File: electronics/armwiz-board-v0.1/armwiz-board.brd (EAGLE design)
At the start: 99.1 x 51.5 mm, 135 parts, among them IC1 STM32F_48PIN, IC2 TXS0108, IC3 TLV70033DCK, J1 MICRO-SDCARD-CONNECTOR-330006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, J15 Cortex Debug, J16 ST-Link v2, J2 CORTEX_DEBUGSMD, Q1 IRLML5103, U1 STM32F10XRXT6, U4 MIC5219-3.3V, X1 FH12-12S-1S, Y1 8MHz, Y3 32.768kHz

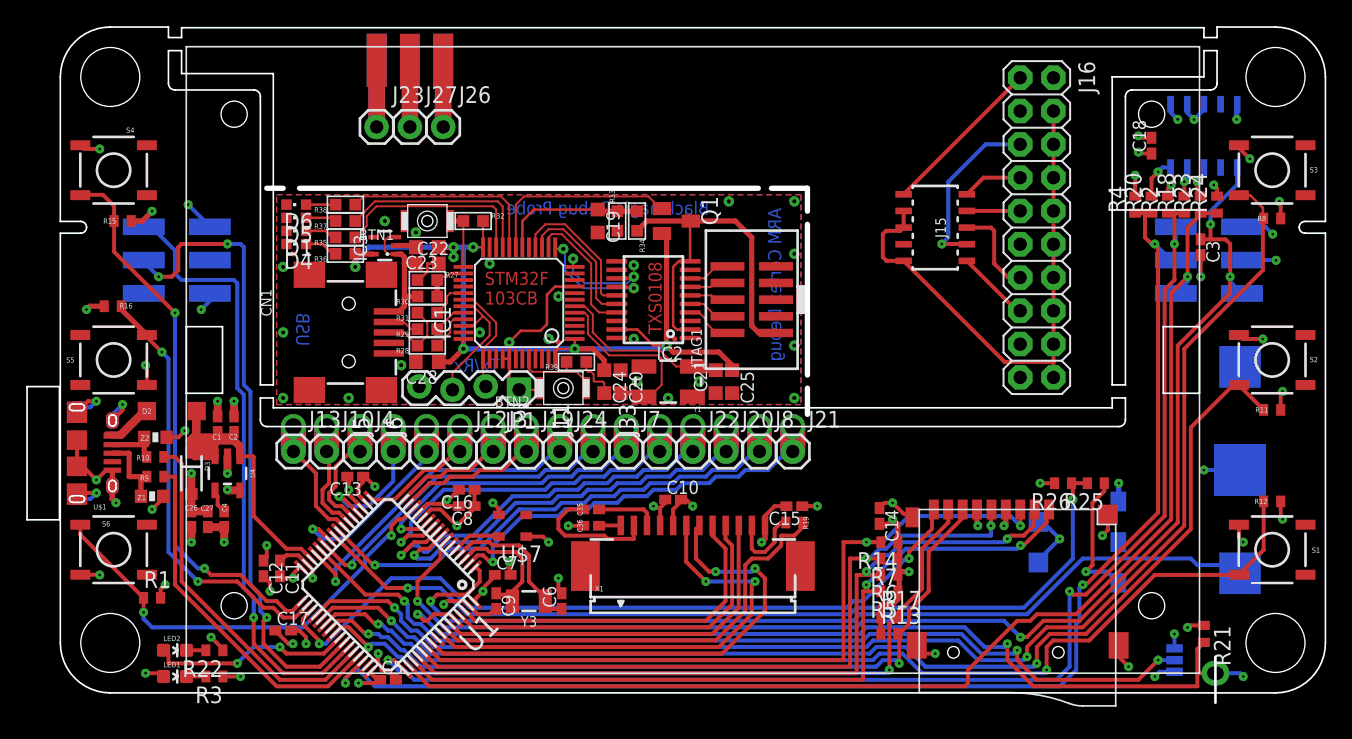
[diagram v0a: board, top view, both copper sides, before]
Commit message: Fixed an issue. Traces were going through the LCD cutout.
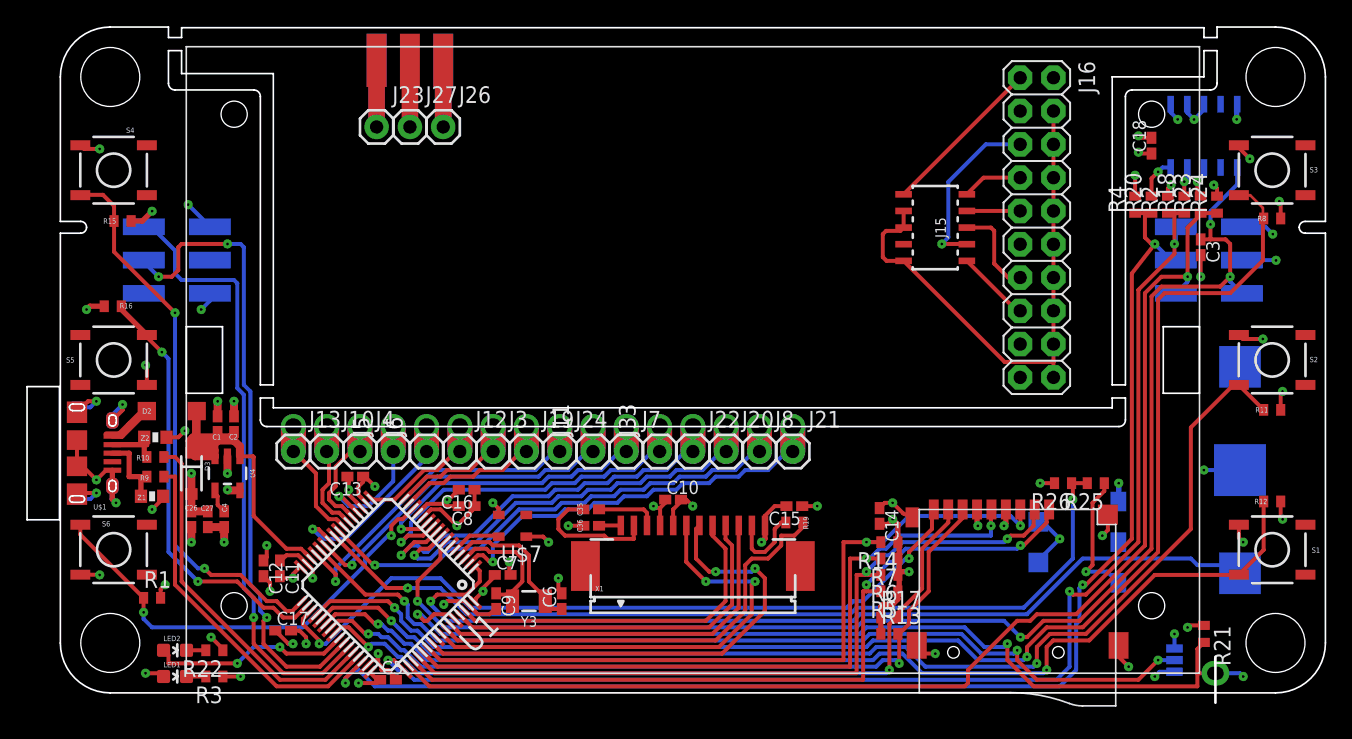
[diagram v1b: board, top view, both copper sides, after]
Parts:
- removed BTN1, BTN2: SPST.B3U-1000P(M)-B, omron:B3U-1000P(M)-B
- removed C19, C24, C25, C28: 100nF, resistor:C0603K
- removed C20, C21: 18pF, resistor:C0603K
- removed C22, C23: 1µF, resistor:C0603K
- removed CN1: (no value), microbuilder_v3:USB-MINIB
- removed D1: RED, led:CHIPLED_0603
- removed D4: GREEN, led:CHIPLED_0603
- removed D5, D6: YELLOW, led:CHIPLED_0603
- removed IC1: STM32F_48PIN, stm32f:TQFP48
- removed IC2: TXS0108, dan-translate:TSSOP20
- removed IC3: TLV70033DCK, tlv700:SC70-5L
- removed JP1: (no value), SparkFun:1X04_LOCK
- removed JTAG1: (no value), microbuilder_v3:2X05_1.27MM_SMT
- removed Q1: IRLML5103, transistor-small-signal:SOT23
- removed R27, R32, R33, R39: 10K, microbuilder:0603-MINI
- removed R28, R29: 22Ω, microbuilder:0603-MINI
- removed R30, R34: 4K7, microbuilder:0603-MINI
- removed R31: 1K5, microbuilder:0603-MINI
- removed R35, R36, R37, R38: 390Ω, microbuilder:0603-MINI
- removed Y1: 8MHz, SparkFun:CRYSTAL-SMD-5X3
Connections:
- removed net 3.3V1: BTN2.2, C23.1, C24.1, C25.1, C28.1, IC1.1, IC1.24, IC1.36, IC1.40, IC1.41, IC1.48, IC1.9, IC2.19, IC3.5, JP1.1, Q1.2, R32.2, R36.1
- removed net 5.0V: C22.1, CN1.VBUS, IC3.1, IC3.3, R30.2
- removed net BOOT2: BTN2.1, IC1.44, R39.2
- removed net D+1: CN1.D+, R28.2, R31.2
- removed net D-1: CN1.D-, R29.2
- removed net FORCE_BOOTLOADER: BTN1.1, IC1.25, R32.1
- removed net GND1: BTN1.2, C19.2, C20.1, C21.1, C22.2, C23.2, C24.2, C25.2, C28.2, CN1.GND, CN1.ID, D1.C, D4.C, D5.C, D6.C, IC1.23, IC1.35, IC1.47, IC1.8, IC2.11, IC2.12, IC2.18, IC2.20, IC3.2, JP1.4, JTAG1.3, JTAG1.5, JTAG1.9, R27.1, R33.1, R39.1
- removed net LED0: IC1.20, R38.1
- removed net LED1: IC1.21, R37.1
- removed net LED2: IC1.22, R35.1
- removed net LPC_XTAL2: C21.2, IC1.6, Y1.1
- removed net N$10: D1.A, R35.2
- removed net N$17: D4.A, R36.2
- removed net N$25: D5.A, R37.2
- removed net N$26: D6.A, R38.2
- removed net OSC_IN1: C20.2, IC1.5, Y1.3
- removed net PWR_BR: IC1.19, Q1.1
- removed net RST: IC1.12, IC2.13
- removed net RXD: IC1.31, IC1.34, JP1.3
- removed net TARGET_POWER_ADC: C19.1, IC1.18, R33.2, R34.1
- removed net TARGET_RST: IC2.8, JTAG1.10
- removed net TARGET_TCK: IC2.5, JTAG1.4
- removed net TARGET_TDI: IC2.7, JTAG1.8
- removed net TARGET_TDO: IC2.6, JTAG1.6
- removed net TARGET_TMS: IC2.4, JTAG1.2
- removed net TCK: IC1.15, IC2.16
- removed net TDI: IC1.13, IC2.14
- removed net TDO: IC1.16, IC2.15
- removed net TMS: IC1.14, IC2.17
- removed net TPWR: IC2.10, IC2.2, JTAG1.1, Q1.3, R34.2
- removed net TXD: IC1.30, IC1.37, JP1.2
- removed net USB_DM: IC1.32, R29.1
- removed net USB_DP: IC1.33, R28.1
- removed net USB_ENUMERATE: IC1.29, R31.1
- removed net VBUS1: IC1.26, R27.2, R30.1
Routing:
- net 3.3V1: track 82.6 -> 0.00 mm, vias 7 -> 0
- net TPWR: track 28.9 -> 0.00 mm
- net LED0: track 15.5 -> 0.00 mm
- net LED2: track 15.2 -> 0.00 mm
- net LED1: track 15.2 -> 0.00 mm
- net PWR_BR: track 15.0 -> 0.00 mm
- net OSC_IN1: track 14.5 -> 0.00 mm
- net LPC_XTAL2: track 13.6 -> 0.00 mm
- net TDO: track 11.2 -> 0.00 mm
- net TARGET_POWER_ADC: track 11.2 -> 0.00 mm
- net TCK: track 10.8 -> 0.00 mm
- net RXD: track 10.6 -> 0.00 mm
- net 5.0V: track 10.4 -> 0.00 mm
- net TMS: track 10.4 -> 0.00 mm
- net TDI: track 9.51 -> 0.00 mm, vias 2 -> 0
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- removed copper zone on layer 1, net GND1
- removed copper zone on layer 16, net GND1
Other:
- outline, holes or cut-outs redrawn
- board text removed: "ARM Cortex Debug"
- board text removed: "Blackmagic Debug Probe"
- board text removed: "STM32F 103CB"
- board text removed: "TXS0108"
- board text removed: "Tx/Rx"
- board text removed: "USB"
